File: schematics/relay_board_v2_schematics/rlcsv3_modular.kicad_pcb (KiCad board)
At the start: 2 copper layers, 45 x 75 mm, 33 parts, among them P1 ACT_PWR, P2 CONN_01X09, P3 ACTUATOR, Q1 MMBF170, Q2 MMBF170, U1 SPST_POWER_RELAY, U2 dpdt_relay, U3 INA180A1, U4 INA180A1

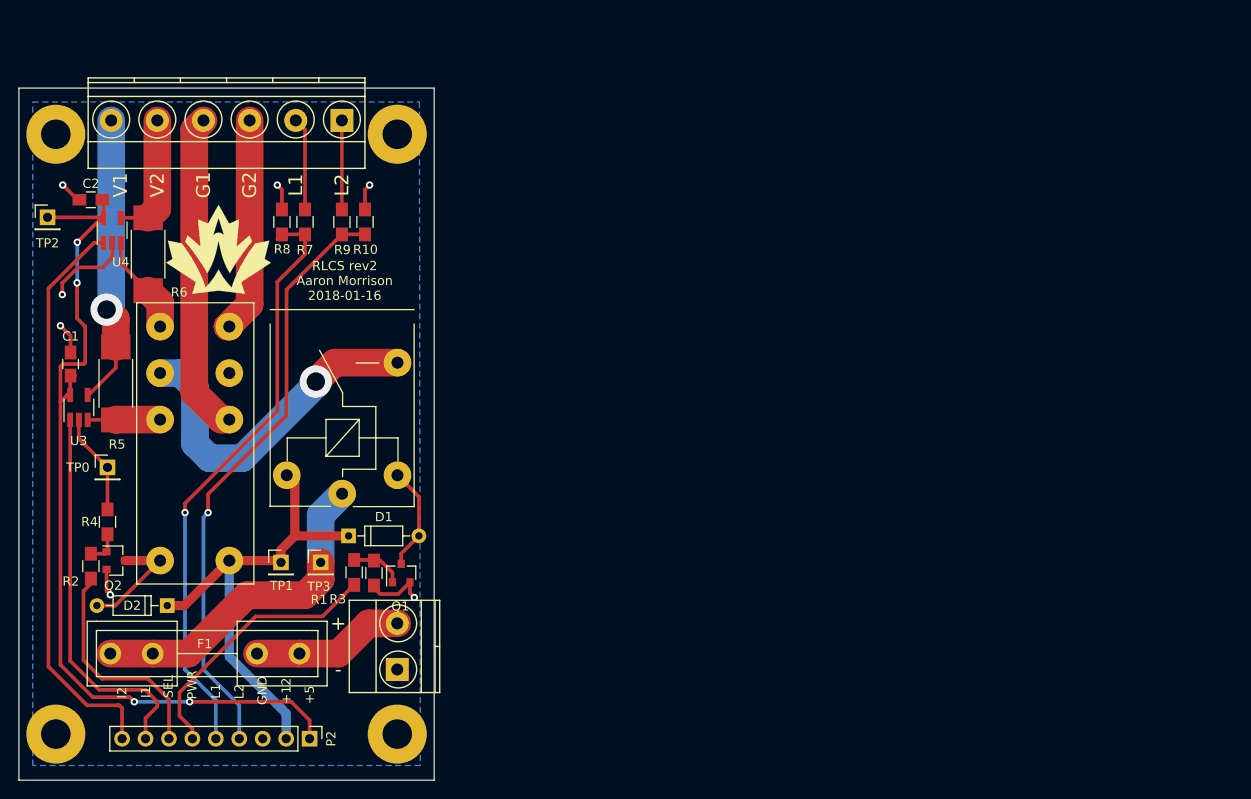
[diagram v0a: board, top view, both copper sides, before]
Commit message: Add initial board layout
Signed-off-by: AIDAN HA <qbha@edu.uwaterloo.ca>
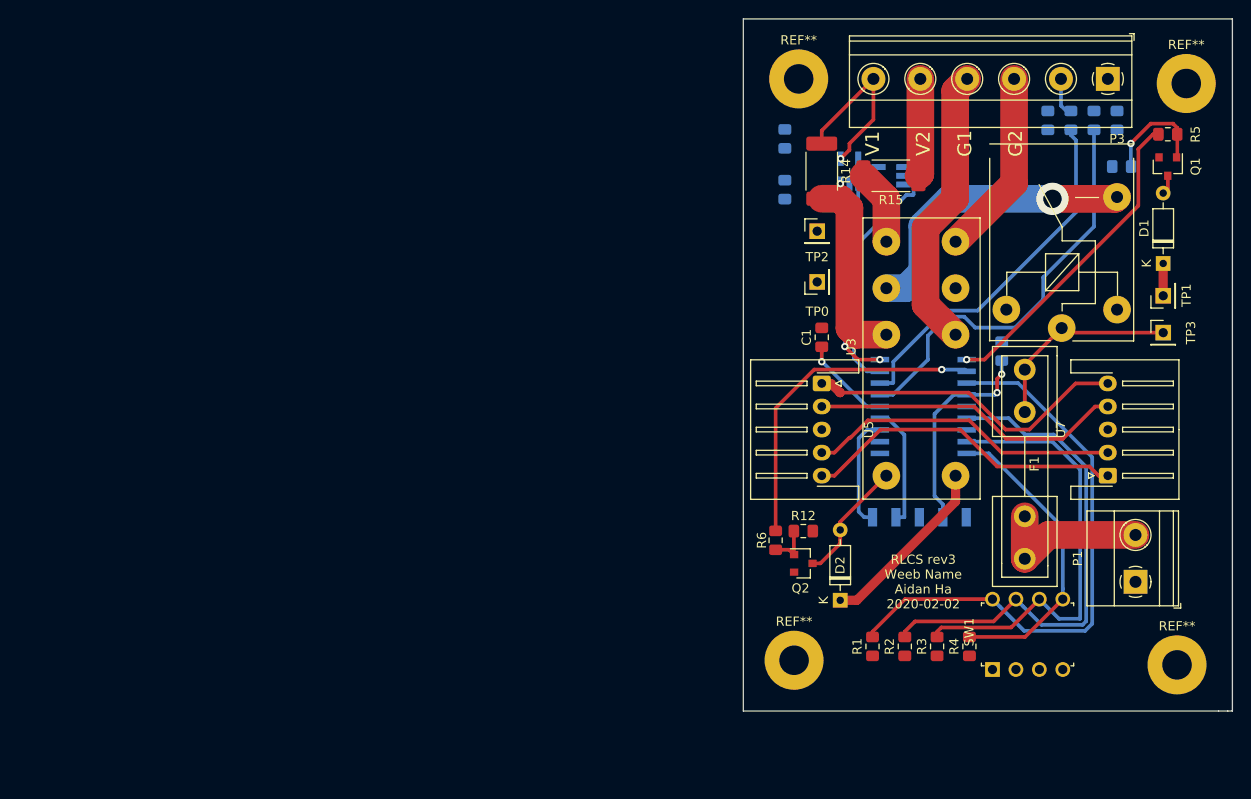
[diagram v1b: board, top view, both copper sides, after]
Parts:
- removed G***: LOGO, custom:rocketry_logo_small_noletters
- removed P2: CONN_01X09, Socket_Strips:Socket_Strip_Straight_1x09_Pitch2.54mm
- removed the REF** at (91.0, 145.0)
- removed the REF** at (54.0, 145.0)
- removed the REF** at (91.0, 80.0)
- removed the REF** at (54.0, 80.0)
- added C3: 0.1uF, Capacitor_SMD:C_0805_2012Metric_Pad1.15x1.40mm_HandSolder, B.Cu at (133.0, 80.5)
- added J1: Programming Header, rlcs:PinHeader_5x2.54_SMD_90deg_952-3198-1-ND, B.Cu at (142.5, 121.5)
- added R11: 10K, Resistor_SMD:R_0805_2012Metric_Pad1.15x1.40mm_HandSolder, B.Cu at (169.5, 83.5)
- added R12: 10K, Resistor_SMD:R_0805_2012Metric_Pad1.15x1.40mm_HandSolder, F.Cu at (135.0, 123.0)
- added R13: 10K, Resistor_SMD:R_0805_2012Metric_Pad1.15x1.40mm_HandSolder, B.Cu at (156.5, 103.5)
- added R14: 0.02, Resistor_SMD:R_2512_6332Metric_Pad1.52x3.35mm_HandSolder, F.Cu at (137.0, 84.0)
- added R15: 0.02, Resistor_SMD:R_2512_6332Metric_Pad1.52x3.35mm_HandSolder, F.Cu at (144.5, 84.5)
- added REF**: MountingHole_3.2mm_M3_Pad, MountingHole:MountingHole_3.2mm_M3_Pad, F.Cu at (175.5, 137.5)
- added REF**: MountingHole_3.2mm_M3_Pad, MountingHole:MountingHole_3.2mm_M3_Pad, F.Cu at (134.0, 137.0)
- added REF**: MountingHole_3.2mm_M3_Pad, MountingHole:MountingHole_3.2mm_M3_Pad, F.Cu at (134.5, 74.0)
- added REF**: MountingHole_3.2mm_M3_Pad, MountingHole:MountingHole_3.2mm_M3_Pad, F.Cu at (176.5, 74.5)
- added SW1: SW_DIP_x04, rlcs:DIP_SWITCH_4X2, F.Cu at (155.5, 138.0)
- added U5: CONN_01x05, Connector_JST:JST_XH_S5B-XH-A-1_1x05_P2.50mm_Horizontal, F.Cu at (137.0, 107.0)
- added U6: INA180A1, Package_TO_SOT_SMD:SOT-23-5_HandSoldering, B.Cu at (144.5, 84.5)
- added U7: CONN_01x05, Connector_JST:JST_XH_S5B-XH-A-1_1x05_P2.50mm_Horizontal, F.Cu at (168.0, 117.0)
- C1: value 0.1uF -> 22uF; footprint Capacitors_SMD:C_0805_HandSoldering -> Capacitor_SMD:C_0805_2012Metric_Pad1.15x1.40mm_HandSolder
- C2: footprint Capacitors_SMD:C_0805_HandSoldering -> Capacitor_SMD:C_0805_2012Metric_Pad1.15x1.40mm_HandSolder; moved to B.Cu
- D1, D2: footprint Diodes_THT:D_DO-35_SOD27_P7.62mm_Horizontal -> Diode_THT:D_DO-35_SOD27_P7.62mm_Horizontal
- F1: footprint custom:littlefuse_01000020Z -> rlcs:littlefuse_01000020Z
- P1: footprint Terminal_Blocks:TerminalBlock_Pheonix_MKDS1.5-2pol -> TerminalBlock_Phoenix:TerminalBlock_Phoenix_MKDS-1,5-2-5.08_1x02_P5.08mm_Horizontal
- P3: footprint Terminal_Blocks:TerminalBlock_Pheonix_MKDS1.5-6pol -> TerminalBlock_Phoenix:TerminalBlock_Phoenix_MKDS-1,5-6-5.08_1x06_P5.08mm_Horizontal
- Q1, Q2: footprint TO_SOT_Packages_SMD:SOT-23 -> Package_TO_SOT_SMD:SOT-23
- R1, R2: value 150 -> 10k; footprint Resistors_SMD:R_0805_HandSoldering -> Resistor_SMD:R_0805_2012Metric_Pad1.15x1.40mm_HandSolder
- R10, R7, R8, R9: footprint Resistors_SMD:R_0805_HandSoldering -> Resistor_SMD:R_0805_2012Metric_Pad1.15x1.40mm_HandSolder; moved to B.Cu
- R3, R4: value 10K -> 10k; footprint Resistors_SMD:R_0805_HandSoldering -> Resistor_SMD:R_0805_2012Metric_Pad1.15x1.40mm_HandSolder
- R5, R6: value 0.02 -> 150; footprint Resistors_SMD:R_2512_HandSoldering -> Resistor_SMD:R_0805_2012Metric_Pad1.15x1.40mm_HandSolder
- U1: footprint custom:Relay_SPST_G5LE-1A -> rlcs:Relay_SPST_G5LE-1A
- U2: value dpdt_relay -> PIC16F1826-ISO; footprint custom:Relay_DPDT_RT424012F -> rlcs:PIC16F1826-ISO; moved to B.Cu
- U3: value INA180A1 -> dpdt_relay; footprint TO_SOT_Packages_SMD:SOT-23-5_HandSoldering -> rlcs:Relay_DPDT_RT424012F
- U4: footprint TO_SOT_Packages_SMD:SOT-23-5_HandSoldering -> Package_TO_SOT_SMD:SOT-23-5_HandSoldering; moved to B.Cu
- moved R5 117.2 mm to (174.5, 80.0), turned to 180 degrees
- moved TP1 99.9 mm to (174.0, 97.5), turned to 90 degrees
- moved TP3 94.6 mm to (174.0, 101.5)
- moved R4 94.4 mm to (153.0, 135.5)
- moved Q1 94.0 mm to (174.5, 83.5), turned to 270 degrees
- moved D1 93.1 mm to (174.0, 94.0), turned to 90 degrees
- moved R2 88.6 mm to (146.0, 135.5), turned to 90 degrees
- moved U3 87.8 mm to (144.0, 117.0)
- moved R9 84.7 mm to (169.0, 78.5)
- moved U2 84.4 mm to (148.0, 109.5), turned to 270 degrees
- moved R7 83.7 mm to (164.0, 78.5)
- moved R8 83.7 mm to (161.5, 78.5)
- moved TP2 83.4 mm to (136.5, 90.5)
- moved P3 83.1 mm to (168.0, 74.0)
- moved C1 81.5 mm to (137.0, 102.0), turned to 90 degrees
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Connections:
- net /Relays/VIN renamed Net-(F1-Pad2)
- C1 pad 1: GND -> +5V
- C1 pad 2: +5V -> GND
- P3 pad 3: /Relays/G2 -> /G2
- P3 pad 4: /Relays/G1 -> /G1
- P3 pad 5: /Relays/P2 -> /P2
- P3 pad 6: /Relays/P1 -> /P1
- R1 pad 1: Net-(Q1-Pad1) -> +5V
- R1 pad 2: POWER -> /DIP_1
- R10 pad 1: LIM2 -> /LIM2
- R2 pad 1: Net-(Q2-Pad1) -> +5V
- R2 pad 2: SELECT -> /DIP_2
- R3 pad 1: Net-(Q1-Pad1) -> +5V
- R3 pad 2: GND -> /DIP_3
- R4 pad 1: Net-(Q2-Pad1) -> +5V
- R4 pad 2: GND -> /DIP_4
- R5 pad 1: /Relays/P1 -> Net-(Q1-Pad1)
- R5 pad 2: Net-(R5-Pad2) -> /POWER
- R6 pad 1: /Relays/P2 -> Net-(Q2-Pad1)
- R6 pad 2: Net-(R6-Pad2) -> /SELECT
- R7 pad 2: LIM1 -> /LIM1
- R8 pad 1: LIM1 -> /LIM1
- R9 pad 2: LIM2 -> /LIM2
- U2 pad 1: Net-(U1-Pad4) -> /POWER
- U2 pad 2: GND -> /SELECT
- U2 pad 3: Net-(D2-Pad2) -> /DIP_1
- U2 pad 4: +12V -> /~MCLR
- U2 pad 5: Net-(R5-Pad2) -> GND
- U2 pad 6: Net-(R6-Pad2) -> /DIP_2
- U2 pad 7: /Relays/G1 -> /SDA
- U2 pad 8: /Relays/G2 -> /DIP_3
- U3 pad 1: CS_1 -> Net-(U1-Pad4)
- U3 pad 3: Net-(R5-Pad2) -> Net-(D2-Pad2)
- U3 pad 4: /Relays/P1 -> +12V
- U3 pad 5: +5V -> Net-(R14-Pad2)
- U4 pad 1: CS_2 -> /CURR_SENSE_1
- U4 pad 3: Net-(R6-Pad2) -> Net-(R14-Pad2)
- U4 pad 4: /Relays/P2 -> /P1
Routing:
- net LIM2: track 65.0 -> 0.00 mm, vias 1 -> 0
- net LIM1: track 64.6 -> 0.00 mm, vias 1 -> 0
- net /DIP_1: track 0.00 -> 62.6 mm
- net CS_2: track 62.2 -> 0.00 mm
- net /DIP_2: track 0.00 -> 54.9 mm
- net +5V: track 97.3 -> 43.8 mm, vias 4 -> 1
- net /DIP_3: track 0.00 -> 48.1 mm
- net /LIM2: track 0.00 -> 45.1 mm
- net CS_1: track 41.9 -> 0.00 mm
- net GND: track 41.8 -> 0.00 mm, vias 7 -> 0
- net /LIM1: track 0.00 -> 39.4 mm
- net /SELECT: track 0.00 -> 35.8 mm, vias 0 -> 1
- net /SDA: track 0.00 -> 35.1 mm
- net /Relays/G1: track 34.9 -> 0.00 mm
- net /POWER: track 0.00 -> 34.5 mm, vias 0 -> 1
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- removed copper zone on B.Cu, net GND
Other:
- board size 45 x 75 mm -> 53 x 75 mm
- board text added: "RLCS rev3 Weeb Name Aidan Ha 2020-02-02"
- board text removed: "+"
- board text removed: "+12"
- board text removed: "+5"
- board text removed: "-"
- board text removed: "GND"
- board text removed: "I1"
- board text removed: "I2"
- board text removed: "L1"
- board text removed: "L2"
- board text removed: "PWR"
- board text removed: "RLCS rev2 Aaron Morrison 2018-01-16"
- board text removed: "SEL"

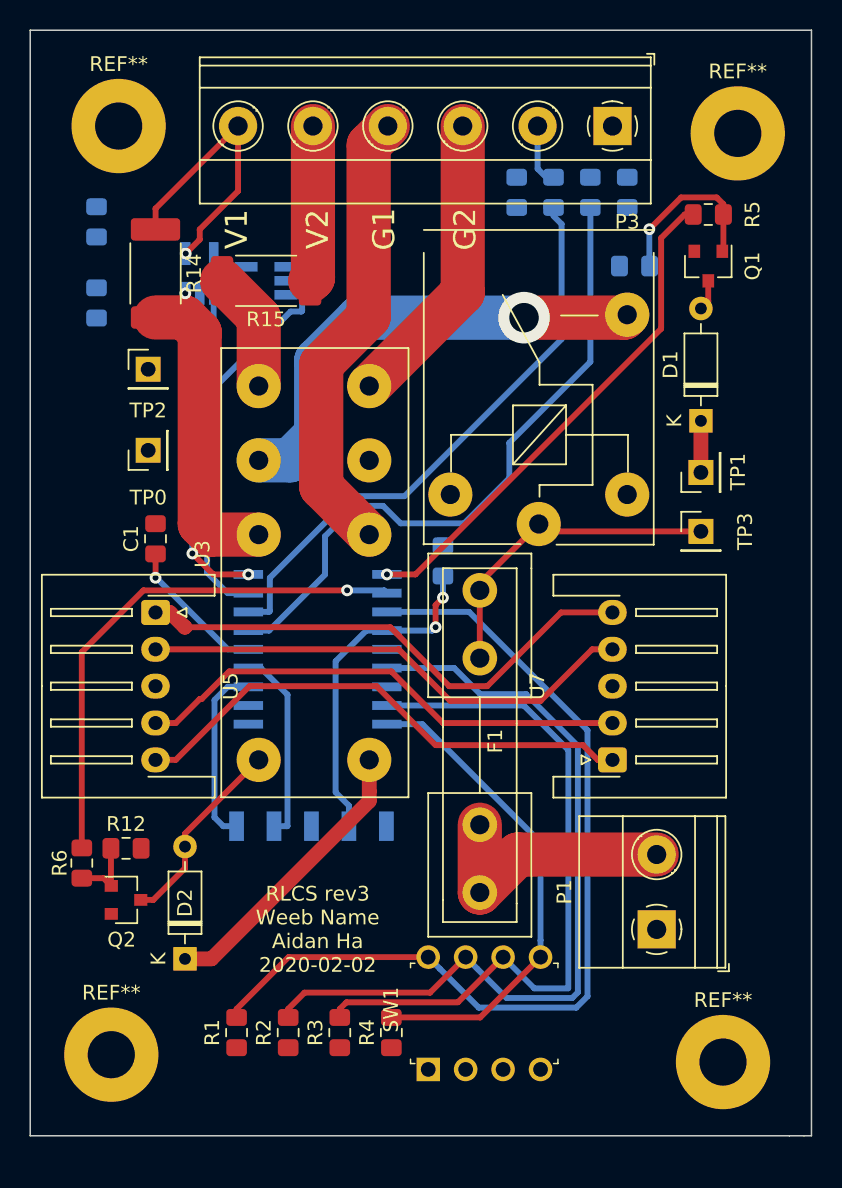
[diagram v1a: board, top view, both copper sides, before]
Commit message: Added traces
Signed-off-by: AIDAN HA <qbha@edu.uwaterloo.ca>
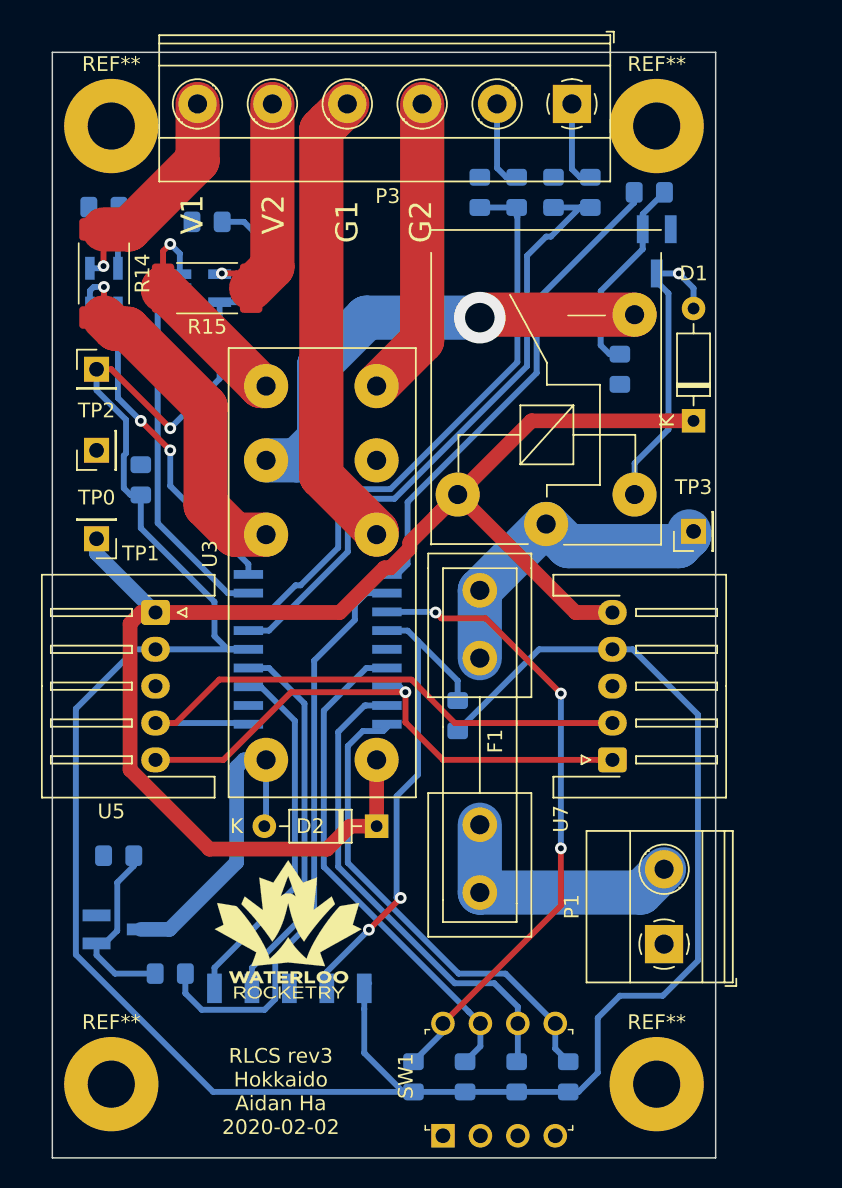
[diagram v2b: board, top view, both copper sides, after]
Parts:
- removed the REF** at (175.5, 137.5)
- removed the REF** at (134.0, 137.0)
- removed the REF** at (134.5, 74.0)
- removed the REF** at (176.5, 74.5)
- added G***: LOGO, rlcs:rocketry_logo_small, F.Cu at (146.0, 128.5)
- added REF**: MountingHole_3.2mm_M3_Pad, MountingHole:MountingHole_3.2mm_M3_Pad, F.Cu at (134.0, 139.0)
- added REF**: MountingHole_3.2mm_M3_Pad, MountingHole:MountingHole_3.2mm_M3_Pad, F.Cu at (171.0, 139.0)
- added REF**: MountingHole_3.2mm_M3_Pad, MountingHole:MountingHole_3.2mm_M3_Pad, F.Cu at (171.0, 74.0)
- added REF**: MountingHole_3.2mm_M3_Pad, MountingHole:MountingHole_3.2mm_M3_Pad, F.Cu at (134.0, 74.0)
- C1, R1, R12, R2, R3, R4, R5, R6: moved to B.Cu
- Q1, Q2: footprint Package_TO_SOT_SMD:SOT-23 -> Package_TO_SOT_SMD:SOT-23_Handsoldering; moved to B.Cu
- moved TP1 41.2 mm to (133.0, 102.0), turned to 180 degrees
- moved D2 15.8 mm to (152.0, 121.5), turned to 180 degrees
- moved R1 12.4 mm to (154.5, 138.5)
- moved R2 12.4 mm to (158.0, 138.5)
- moved R3 12.4 mm to (161.5, 138.5)
- moved R4 12.4 mm to (165.0, 138.5)
- moved J1 11.1 mm to (141.0, 132.5)
- moved R13 10.5 mm to (157.5, 114.0), turned to 90 degrees
- moved R6 9.60 mm to (138.0, 131.5), turned to 0 degrees
- moved C3 7.50 mm to (140.5, 80.5), turned to 0 degrees
- moved R11 7.07 mm to (168.5, 90.5), turned to 270 degrees
- moved U4 6.58 mm to (133.5, 85.0)
- moved C2 6.52 mm to (133.5, 79.5), turned to 0 degrees
- moved SW1 4.61 mm to (156.5, 142.5)
- moved U6 4.53 mm to (140.0, 85.0), turned to 0 degrees
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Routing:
- net +5V: track 43.8 -> 183.3 mm
- net +12V: track 58.4 -> 100.8 mm
- net /DIP_2: track 54.9 -> 34.1 mm
- net /DIP_1: track 62.6 -> 43.2 mm, vias 0 -> 3
- net Net-(D1-Pad2): track 2.09 -> 20.6 mm, vias 0 -> 1
- net /DIP_3: track 48.1 -> 33.1 mm
- net /ICSPDAT: track 13.2 -> 26.5 mm
- net /ICSPCLK: track 12.4 -> 24.5 mm
- net /~MCLR: track 23.0 -> 34.1 mm
- net Net-(D2-Pad2): track 13.3 -> 23.0 mm
- net Net-(Q2-Pad1): track 4.78 -> 12.6 mm
- net Net-(R15-Pad2): track 8.17 -> 15.4 mm, vias 0 -> 1
- net /SCL: track 33.9 -> 39.9 mm
- net Net-(P3-Pad1): track 0.00 -> 5.90 mm
- net /P2: track 10.6 -> 15.7 mm, vias 0 -> 1
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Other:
- board size 53 x 75 mm -> 45 x 75 mm
- board text added: "RLCS rev3 Hokkaido Aidan Ha 2020-02-02"
- board text removed: "RLCS rev3 Weeb Name Aidan Ha 2020-02-02"
